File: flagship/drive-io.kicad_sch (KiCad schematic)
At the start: 11 parts, among them J4 DRIVE_COMMS, J5 DRIVE_MOTION, U10 74AHCT125, U9 THVD1450

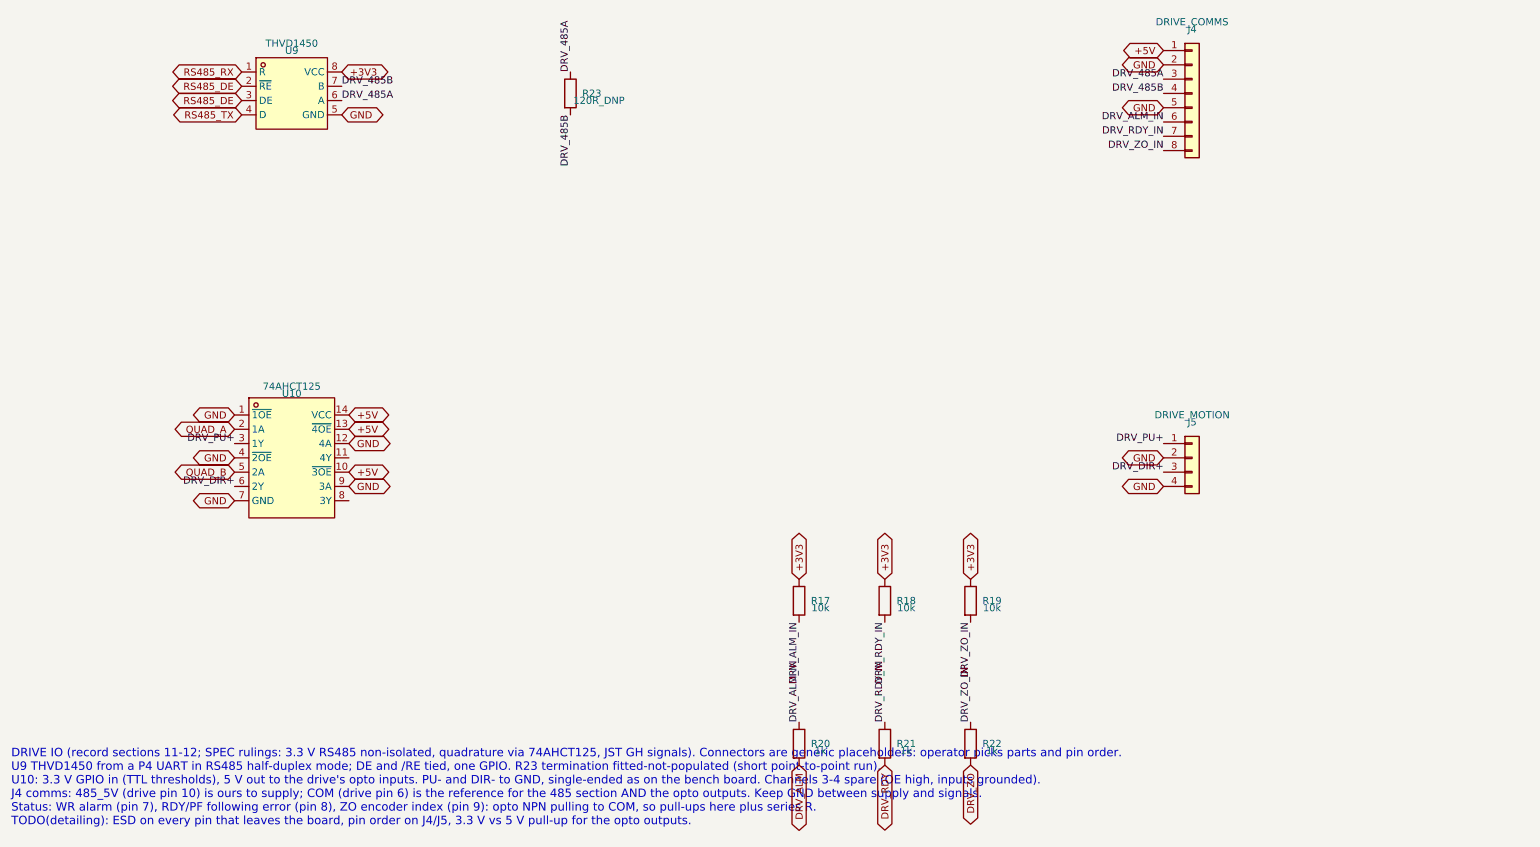
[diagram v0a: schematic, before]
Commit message: flagship: rails detailed per the TPS54560B datasheet; logic power moved to the stamp's own rails
Rails: three identical 400 kHz columns (A3 sheet), 4 A each, VIN 20-48 V, UVLO 20/17 V,
values from the datasheet design procedure (inductor, derated ceramic output, FB, type-II
comp, B560C catch diode, 4x 2.2u/100V input). Worst on-time 205 ns vs 135 ns minimum.
Logic power (operator): +5V_SYS = stamp pad 39 (VIN/USB OR) feeds the 74AHCT125, drive
485_5V and status LED, so USB alone emits quadrature; +3V3_SYS = stamp pad 28 feeds the
INA228, THVD1450 and all pull-ups. 3.3 V buck is accessory-only (+3V3_ACC). Netlist checked:
the five power domains are separate. SPEC rulings recorded.

Co-Authored-By: Claude Opus 5.5 (1M context) <noreply@anthropic.com>
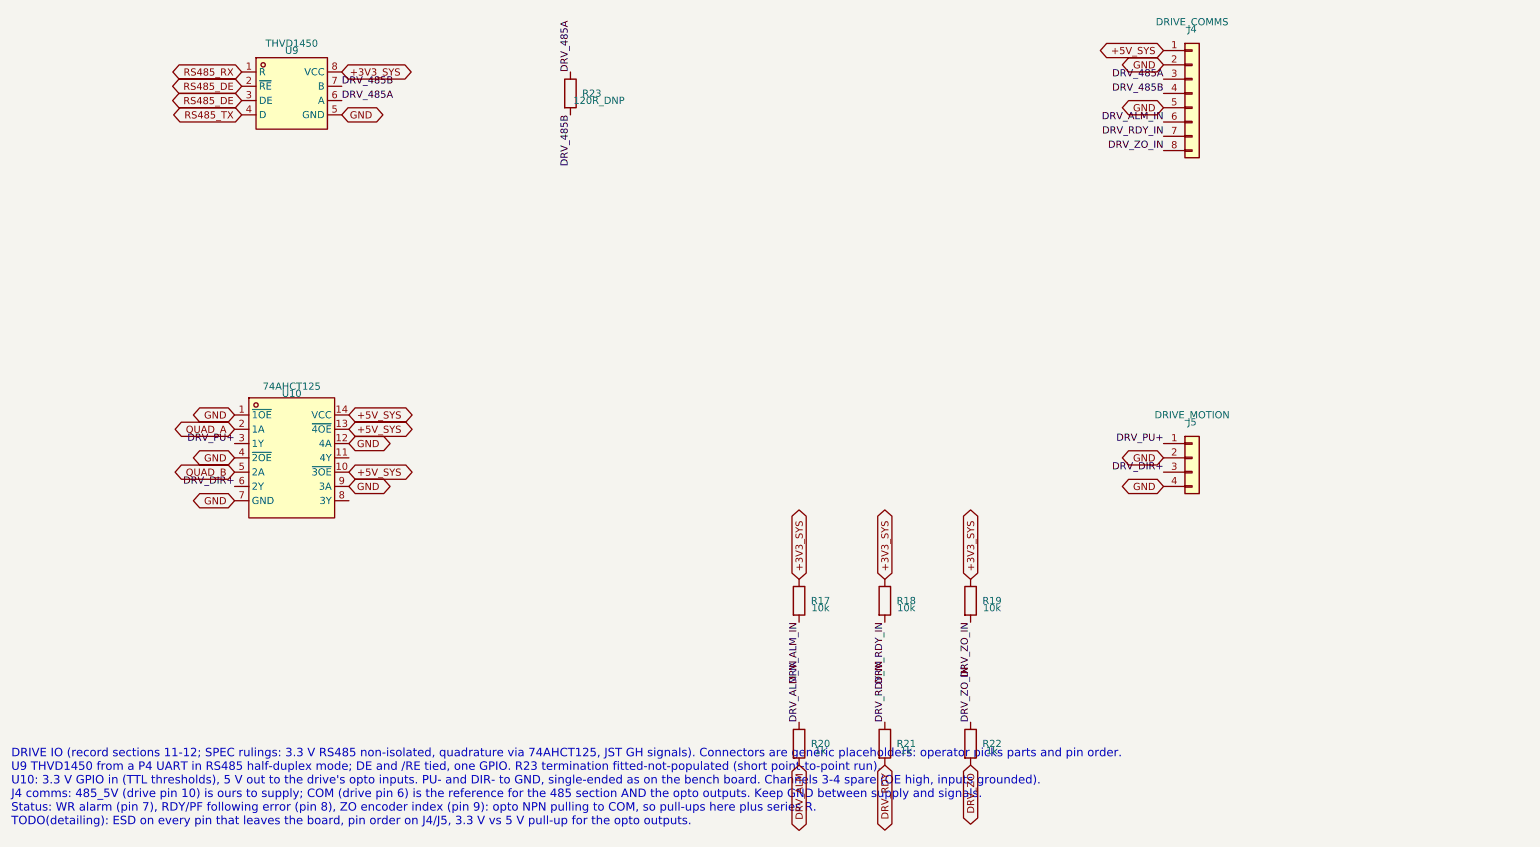
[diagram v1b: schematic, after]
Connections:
- net +3V3 renamed +3V3_SYS
- net +5V renamed +5V_SYS
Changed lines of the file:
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@@
 		)
 	)
-	(global_label "+5V"
+	(global_label "+5V_SYS"
 		(shape bidirectional)
 		(at 80.01 116.84 0)
@@
 		)
 	)
-	(global_label "+5V"
+	(global_label "+5V_SYS"
 		(shape bidirectional)
 		(at 224.79 52.07 180)
@@
 		)
 	)
-	(global_label "+3V3"
+	(global_label "+3V3_SYS"
 		(shape bidirectional)
 		(at 160.02 146.05 90)
@@
 		)
 	)
-	(global_label "+3V3"
+	(global_label "+3V3_SYS"
 		(shape bidirectional)
 		(at 175.26 146.05 90)
@@
 		)
 	)
-	(global_label "+5V"
+	(global_label "+5V_SYS"
 		(shape bidirectional)
 		(at 80.01 127 0)
@@
 		)
 	)
-	(global_label "+3V3"
+	(global_label "+3V3_SYS"
 		(shape bidirectional)
 		(at 78.74 55.88 0)
@@
 		)
 	)
-	(global_label "+5V"
+	(global_label "+5V_SYS"
 		(shape bidirectional)
 		(at 80.01 119.38 0)
@@
 		)
 	)
-	(global_label "+3V3"
+	(global_label "+3V3_SYS"
 		(shape bidirectional)
 		(at 190.5 146.05 90)
